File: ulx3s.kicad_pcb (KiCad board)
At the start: 4 copper layers, 139.6 x 119.6 mm, 274 parts, among them IC101 TPD4E001DRLR, IC102 74AUP1G74DC.125, IC103 CD74HC4050PWR, IC104 STM32F769IIT6, IC105 LD1117ADT33TR, IC106 N.C., IC107 IS42S16400J, IC108 AT24C256C-SSHL-B, IC109 TPS2051BDBVR, IC110 TPS61169DCKR, IC111 TPD4E001DRLR, IC112 TSC2007IPW, IC113 N.C., IC114 DP83848CVV_NOPB, J101 503398-1892, J102 67803-8020, J4 CONN_02X03, Q101 N.C., Q102 2N7002, SW101 TL1100CF160Q, SW102 PEC16-2215F-S0024, U1 LFE5U-85F-6BG381C, U10 IS25LP128F-JBLE, U3 TLV62569DBV, U4 TLV62569DBV, U5 TLV62569DBV, X101 DS1024-2*20R0, X102 DS1013-16SSIB1, X103 691322110005, X104 N.C., X105 LMJTAB881243M-L, Y1 FNETHE025, Y101 25MHz, Y102 XTAL016178-85SMX

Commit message: Adding dimensions
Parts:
- moved D20 149.3 mm to (199.9, -6.33)
- moved D21 149.3 mm to (206.2, -6.44)
- moved D23 149.3 mm to (195.1, -4.93)
- moved D24 149.3 mm to (195.1, -6.84)
- moved D25 149.3 mm to (209.7, -3.65)
- moved D26 149.3 mm to (211.6, -3.65)
- moved R52 149.3 mm to (203.8, -7.84)
- moved R53 149.3 mm to (202.4, -7.84)
- moved R54 149.3 mm to (206.0, -9.49)
- moved R63 149.3 mm to (199.9, -7.86)
- moved US2 149.3 mm to (202.7, -11.7)
- moved D9 149.3 mm to (206.7, 0.63)
- moved GPDI1 149.3 mm to (165.8, -6.75)
- moved R40 149.3 mm to (199.9, -9.25)
- moved R64 149.3 mm to (206.0, -8.09)
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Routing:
- net +5V: track 35.7 -> 258.7 mm
- net +12V: track 0.00 -> 136.6 mm
- net PE: track 0.00 -> 40.8 mm
- net GND: vias 82 -> 270
- net +3V3: vias 16 -> 37
- net USER_SW: vias 0 -> 1
- net N$124: vias 0 -> 1
- net FRM3: vias 0 -> 1
- net EOUT_B: vias 0 -> 1
- added copper zone on B.Cu, net +3V3
- added copper zone on F.Cu, net +3V3
- added copper zone on In2.Cu, net +3V3
- added copper zone on F.Cu, net +5V
- added copper zone on In2.Cu, net +5V
- added copper zone on In1.Cu, net GND
- added copper zone on F.Cu, net Net-(D2-PadA)
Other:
- board size 139.6 x 119.6 mm -> 139.5 x 70 mm
- board text added: "1"
- board text added: "1 Vdd target 2 SWCLK 3 Gnd 4 SWDIO 5 !RESET! 6 SWO"
- board text added: "2"
- board text added: "3"
- board text added: "4"
- board text added: "EEZ DIB MCU (10/2020 r3B4)"
- board text added: "EEZ DIB MCU (10/2020 r3B4) Project source code: github.com/eez-open/modular-psu"

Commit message: Combined
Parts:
- C117, C131, C133, RN2: moved to B.Cu
- moved C13 71.2 mm to (144.3, 74.0)
- moved J4 68.2 mm to (157.3, 105.5), turned to 180 degrees
- moved C1 66.4 mm to (138.8, 80.1)
- moved C2 66.4 mm to (171.2, 99.2)
- moved C3 66.4 mm to (171.4, 92.9)
- moved C30 66.4 mm to (151.2, 93.3)
- moved C4 66.4 mm to (171.4, 94.8)
- moved C42 66.4 mm to (155.1, 78.0)
- moved C46 66.4 mm to (163.2, 103.9)
- moved C48 66.4 mm to (139.1, 82.9)
- moved C53 66.4 mm to (140.7, 87.2)
- moved D28 66.4 mm to (171.7, 86.4)
- moved L3 66.4 mm to (172.7, 77.0)
- moved R11 66.4 mm to (133.9, 100.4)
- moved R27 66.4 mm to (145.4, 98.4)
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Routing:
- net +5V: track 258.7 -> 159.5 mm
- net +12V: track 136.6 -> 37.4 mm
- net JTAG_TDI: track 12.6 -> 7.73 mm, vias 3 -> 2
- net JTAG_TMS: track 11.0 -> 6.28 mm, vias 2 -> 1
- net JTAG_TCK: track 11.8 -> 7.39 mm, vias 2 -> 1
- net /gpio/OUT5V: track 4.31 -> 0.00 mm, vias 1 -> 0
- net JTAG_TDO: track 9.95 -> 5.69 mm, vias 3 -> 2
- net /gpio/IN5V: track 18.9 -> 15.3 mm
- net Net-(D26-Pad1): track 7.59 -> 4.94 mm
- net USB_FPGA_PULL_D-: track 2.47 -> 0.57 mm
- net Net-(D25-Pad2): track 4.76 -> 3.36 mm
- net 2V5_3V3: track 28.2 -> 28.0 mm, vias 4 -> 2
- net SPI2_CSB: track 0.05 -> 0.00 mm, vias 1 -> 0
- net GND: vias 270 -> 212
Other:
- board size 139.5 x 70 mm -> 139.5 x 110.4 mm

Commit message: Board update
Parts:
- C101, C103, C104, C106, C108, C109, C125, C132, C133, C135, C136, C138, C139, C151, C153, C158: footprint EEZ DIB MCU r3B4:C0805 -> Capacitor_SMD:C_0805_2012Metric
- C105, C107, C110, C111, C112, C113, C114, C116, C117, C118, C119, C120, C121, C122, C123, C124, C126, C127, C128, C129, C130, C131, C134, C137, C140, C142, C143, C144, C145, C146, C147, C148, C149, C155, C157, C159, C160, C161, C162, C163, C164, C165, C167, C168, C169, C170: footprint EEZ DIB MCU r3B4:C0603 -> Capacitor_SMD:C_0603_1608Metric
- C141, C150, C156: footprint EEZ DIB MCU r3B4:C1206 -> Capacitor_SMD:C_1206_3216Metric
- C152, C166: footprint EEZ DIB MCU r3B4:EC1206 -> Capacitor_SMD:C_1206_3216Metric
- C154: footprint EEZ DIB MCU r3B4:C1812 -> Capacitor_SMD:C_1812_4532Metric
- D20, D21, D23, D24, D25, D26, D28, D29: footprint Diode_SMD:D_SOD-323_HandSoldering -> Diode_SMD:D_SOD-323
- IC104: footprint EEZ DIB MCU r3B4:LQFP-176_24X24MM -> Package_QFP:LQFP-176_24x24mm_P0.5mm
- IC107: footprint EEZ DIB MCU r3B4:TSOPII-54 -> Package_SO:TSOP-II-54_22.2x10.16mm_P0.8mm
- R101, R102, R103, R104, R105, R106, R107, R108, R109, R110, R111, R112, R113, R114, R115, R116, R117, R118, R119, R120, R121, R122, R123, R124, R125, R126, R127, R128, R129, R130, R131, R132, R133, R134, R135, R136, R137, R138, R139, R140, R141, R142, R143, R144, R145, R146, R147, R148, R149, R150, R151: footprint EEZ DIB MCU r3B4:R0805 -> Resistor_SMD:R_0805_2012Metric
- moved R142 64.6 mm to (90.0, 50.9), turned to 270 degrees
- moved JP110 62.4 mm to (98.6, 49.6), turned to 0 degrees
- moved R140 62.0 mm to (90.0, 54.8), turned to 270 degrees
- moved JP108 60.9 mm to (98.6, 51.6), turned to 180 degrees
- moved R137 59.7 mm to (90.0, 58.8), turned to 90 degrees
- moved JP109 59.4 mm to (98.6, 53.6), turned to 180 degrees
- moved JP111 58.0 mm to (98.6, 55.6), turned to 180 degrees
- moved D21 57.3 mm to (166.3, 48.4)
- moved D23 57.3 mm to (161.1, 51.9)
- moved D25 57.3 mm to (165.3, 51.7)
- moved D26 57.3 mm to (167.2, 51.7)
- moved D9 57.3 mm to (161.6, 56.0)
- moved R52 57.3 mm to (163.9, 47.0)
- moved R53 57.3 mm to (162.5, 47.0)
- moved R54 57.3 mm to (166.2, 45.4)
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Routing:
- net +12V: track 37.4 -> 14.0 mm
- net +5V: track 159.5 -> 139.0 mm
- net +2V5: track 92.7 -> 103.0 mm
- net +3V3: track 88.4 -> 84.5 mm
- net Net-(D26-Pad1): track 4.94 -> 1.72 mm
- net USB_FPGA_PULL_D+: track 7.45 -> 5.54 mm
- net GND: vias 212 -> 202
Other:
- board size 139.5 x 110.4 mm -> 139.5 x 91.8 mm

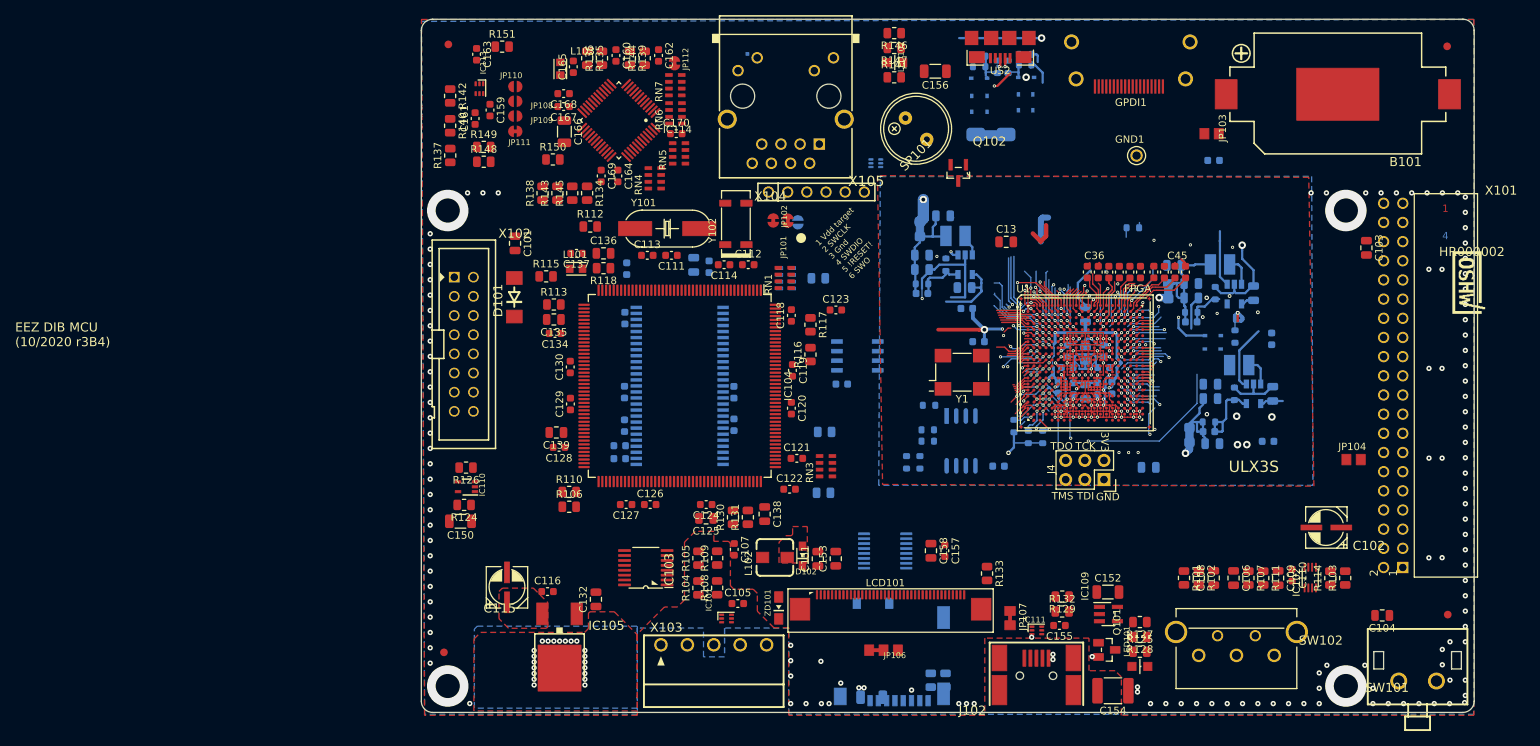
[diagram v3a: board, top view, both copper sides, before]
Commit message: Update 3D models, start to send pins to FPGA
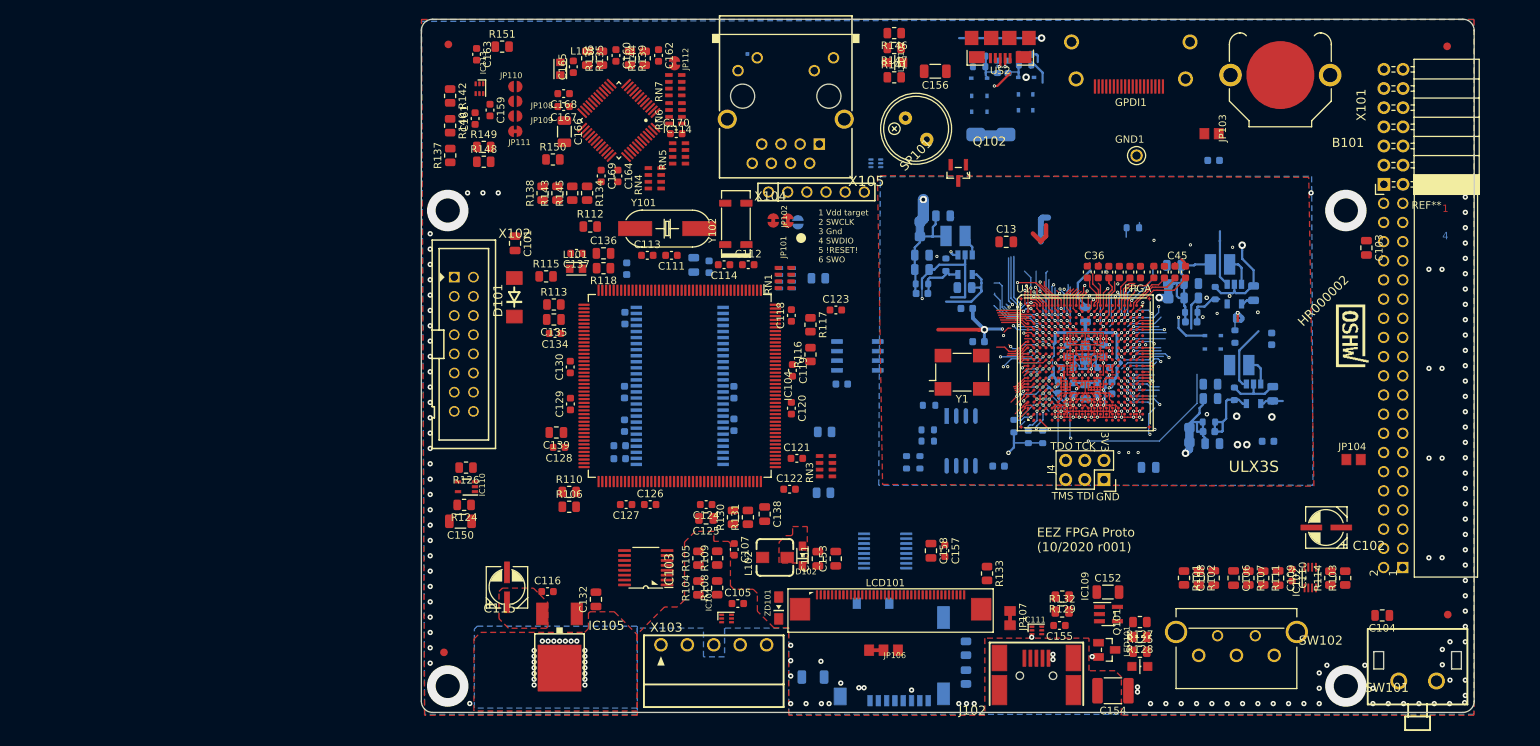
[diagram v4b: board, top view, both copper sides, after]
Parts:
- added REF**: PinSocket_2x07_P2.54mm_Horizontal, Connector_PinSocket_2.54mm:PinSocket_2x07_P2.54mm_Horizontal, F.Cu at (213.7, 62.6)
- B101: value DS1092-10-W6L -> BatteryHolder_Keystone_3001_1x12mm; footprint EEZ DIB MCU r3B4:DS1092-10-W6L -> Battery:BatteryHolder_Keystone_3001_1x12mm
- moved LABEL1 17.0 mm to (207.3, 82.7)
- moved C141 8.23 mm to (138.0, 127.9)
- moved B101 8.03 mm to (200.0, 48.1)
- moved R122 6.30 mm to (158.3, 124.1)
- moved R123 2.74 mm to (158.3, 127.9)
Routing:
- net GND: vias 202 -> 194
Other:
- board text added: "EEZ FPGA Proto (10/2020 r001)"
- board text removed: "EEZ DIB MCU (10/2020 r3B4)"

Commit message: Update
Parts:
- removed REF**: PinSocket_2x07_P2.54mm_Horizontal, Connector_PinSocket_2.54mm:PinSocket_2x07_P2.54mm_Horizontal
- removed RN1, RN2, RN7: DR1206-33R-4/8, EEZ DIB MCU r3B4:CAY16
- added H1: HOLE, MountingHole:MountingHole_3.2mm_M3_ISO14580_Pad, F.Cu at (89.7, 66.2)
- added H2: HOLE, MountingHole:MountingHole_3.2mm_M3_ISO14580_Pad, F.Cu at (208.6, 66.2)
- added H3: HOLE, MountingHole:MountingHole_3.2mm_M3_ISO14580_Pad, F.Cu at (208.6, 129.1)
- added H4: HOLE, MountingHole:MountingHole_3.2mm_M3_ISO14580_Pad, F.Cu at (89.5, 129.1)
- added RN101: DR1206-33R-4/8, EEZ DIB MCU r3B4:CAY16, F.Cu at (134.3, 75.0)
- added RN102: DR1206-33R-4/8, EEZ DIB MCU r3B4:CAY16, B.Cu at (134.4, 75.0)
- added RN103: DR1206-33R-4/8, EEZ DIB MCU r3B4:CAY16, F.Cu at (109.1, 108.5)
- added RN107: DR1206-33R-4/8, EEZ DIB MCU r3B4:CAY16, F.Cu at (102.7, 68.4)
- B101: value BatteryHolder_Keystone_3001_1x12mm -> DS1092-10-W6L; footprint Battery:BatteryHolder_Keystone_3001_1x12mm -> EEZ DIB MCU r3B4:DS1092-10-W6L
- C152: footprint Capacitor_SMD:C_1206_3216Metric -> Capacitor_Tantalum_SMD:CP_EIA-3216-10_Kemet-I
- C166: value 10u -> 10uF; footprint Capacitor_SMD:C_1206_3216Metric -> Capacitor_Tantalum_SMD:CP_EIA-3216-10_Kemet-I
- R101, R102, R103, R104, R105, R106, R107, R108, R109, R110, R111, R112, R113, R114, R115, R122, R123, R124, R125, R126, R127, R128, R132, R133, R137, R146, R147: footprint Resistor_SMD:R_0805_2012Metric -> Resistor_SMD:R_0603_1608Metric
- RN105: renamed from RN5; moved to B.Cu
- moved R149 28.6 mm to (123.0, 59.5), turned to 45 degrees
- moved IC113 24.3 mm to (112.8, 65.1), turned to 180 degrees
- moved R116 22.8 mm to (151.2, 66.8), turned to 180 degrees
- moved RN106 20.4 mm to (106.2, 68.4), turned to 180 degrees
- moved IC112 19.9 mm to (166.8, 116.3), turned to 0 degrees
- moved R117 18.3 mm to (151.4, 69.1), turned to 180 degrees
- moved R112 16.8 mm to (119.5, 55.5)
- moved R134 15.2 mm to (120.0, 54.2), turned to 0 degrees
- moved C157 14.5 mm to (142.5, 104.8)
- moved C123 12.6 mm to (146.6, 68.0)
- moved R133 11.8 mm to (172.9, 113.9)
- moved C158 11.5 mm to (142.5, 108.3)
- moved RN104 9.67 mm to (110.1, 68.4), turned to 0 degrees
- moved C11 8.49 mm to (150.6, 82.2)
- moved C17 8.49 mm to (172.2, 98.3)
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- renumbered RN4 to RN104, RN6 to RN106
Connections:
- C152 pad 1: (no net) -> Net-(C152-Pad1)
- C152 pad 2: (no net) -> GND
- C155 pad 2: Net-(C152-Pad+) -> Net-(C152-Pad1)
- C166 pad 1: (no net) -> Net-(C164-Pad1)
- C166 pad 2: (no net) -> GND
- IC104 pad 11: LTDC_VSYNC -> LED3
- IC104 pad 114: LTDC_R7 -> LED1
- IC104 pad 115: LTDC_CLK -> GP12
- IC104 pad 12: LTDC_HSYNC -> LED2
- IC104 pad 121: SDMMC1_D0 -> (no net)
- IC104 pad 123: SPI2_IRQ -> (no net)
- IC104 pad 13: LTDC_G6 -> LED0
- IC104 pad 132: LTDC_G5 -> GP11
- IC104 pad 138: SPI5_IRQ -> (no net)
- IC104 pad 141: SDMMC1_CK -> (no net)
- IC104 pad 144: SDMMC1_CMD -> (no net)
- IC104 pad 145: LTDC_G7 -> GP9
- IC104 pad 153: LTDC_G3 -> GP10
- IC104 pad 154: LTDC_B3 -> GN11
- IC104 pad 155: LTDC_B4 -> AUDIO_V2
- IC104 pad 156: SPI5_CSB -> (no net)
- IC104 pad 157: SD_DETECT -> (no net)
- IC104 pad 160: FMC_SDNCAS -> (no net)
- IC104 pad 168: SPI4_IRQ -> (no net)
- IC104 pad 174: LTDC_B5 -> AUDIO_R2
- IC104 pad 175: LTDC_B6 -> AUDIO_L1
- IC104 pad 176: LTDC_B7 -> GN10
- IC104 pad 28: LTDC_DE -> AUDIO_L0
- IC104 pad 32: LTDC_R5 -> LED6
- IC104 pad 4: SPI4_MISO -> (no net)
- IC104 pad 45: LTDC_G4 -> AUDIO_L2
- IC104 pad 51: LTDC_R4 -> LED4
- IC104 pad 52: LTDC_G2 -> AUDIO_R0
- IC104 pad 56: LTDC_R3 -> LED7
- IC104 pad 57: LTDC_R6 -> GN9
- IC104 pad 87: SPI2_MISO -> (no net)
- IC107 pad 17: FMC_SDNCAS -> (no net)
- IC109 pad 1: Net-(C152-Pad+) -> Net-(C152-Pad1)
- IC111 pad 6: Net-(C152-Pad+) -> Net-(C152-Pad1)
- J101 pad 3: SDMMC1_CMD -> SDMMC1_FROM_FPGA_CMD
- J101 pad 5: SDMMC1_CK -> (no net)
- J101 pad 7: SDMMC1_D0 -> SDMMC1_FROM_FPGA_D0
- J101 pad SW1: SD_DETECT -> (no net)
- J102 pad 1: Net-(C152-Pad+) -> Net-(C152-Pad1)
- LCD101 pad 10: LTDC_R5 -> FTDI_nRXLED
- LCD101 pad 11: LTDC_R6 -> LTDC_FROM_FPGA_R6
- LCD101 pad 12: LTDC_R7 -> LTDC_FROM_FPGA_R7
- LCD101 pad 15: LTDC_G2 -> FTDI_TXDEN
- LCD101 pad 16: LTDC_G3 -> LTDC_FROM_FPGA_G3
- LCD101 pad 17: LTDC_G4 -> LTDC_FROM_FPGA_G4
- LCD101 pad 18: LTDC_G5 -> FTDI_RXD
- LCD101 pad 19: LTDC_G6 -> LTDC_FROM_FPGA_G6
- LCD101 pad 20: LTDC_G7 -> LTDC_FROM_FPGA_G7
- LCD101 pad 24: LTDC_B3 -> LTDC_FROM_FPGA_B3
- LCD101 pad 25: LTDC_B4 -> LTDC_FROM_FPGA_B4
- LCD101 pad 26: LTDC_B5 -> LTDC_FROM_FPGA_B5
- LCD101 pad 27: LTDC_B6 -> LTDC_FROM_FPGA_B6
- LCD101 pad 28: LTDC_B7 -> LTDC_FROM_FPGA_B7
- LCD101 pad 30: LTDC_CLK -> LTDC_FROM_FPGA_CLK
- LCD101 pad 32: LTDC_HSYNC -> BTN_L
- LCD101 pad 33: LTDC_VSYNC -> BTN_D
- LCD101 pad 34: LTDC_DE -> LTDC_FROM_FPGA_DE
- LCD101 pad 8: LTDC_R3 -> LTDC_FROM_FPGA_R3
- LCD101 pad 9: LTDC_R4 -> LTDC_FROM_FPGA_R4
- R122 pad 2: SDMMC1_D0 -> SDMMC1_FROM_FPGA_D0
- R123 pad 2: SDMMC1_CMD -> SDMMC1_FROM_FPGA_CMD
- R128 pad 1: Net-(C152-Pad+) -> Net-(C152-Pad1)
- R129 pad 1: Net-(C152-Pad+) -> Net-(C152-Pad1)
- RN3 pad 1: SPI2_CSB -> (no net)
- RN3 pad 2: SPI2_CLK -> (no net)
- RN3 pad 3: SPI2_MOSI -> (no net)
- RN3 pad 4: SPI2_CSA -> (no net)
- RN3 pad 5: Net-(IC104-Pad162) -> (no net)
- U1 pad A2: (no net) -> GP9
- U1 pad A3: (no net) -> AUDIO_R0
- U1 pad B1: (no net) -> GN9
- U1 pad B2: (no net) -> LED0
- U1 pad B4: (no net) -> GN10
- U1 pad C1: (no net) -> LED2
- U1 pad C2: (no net) -> LED1
- U1 pad C3: (no net) -> AUDIO_L2
- U1 pad C4: (no net) -> GP10
- U1 pad D1: (no net) -> LED4
- U1 pad D2: (no net) -> LED3
- U1 pad D3: (no net) -> AUDIO_L1
- U1 pad D5: (no net) -> AUDIO_R2
- U1 pad E1: (no net) -> LED6
- U1 pad E3: (no net) -> GN11
- U1 pad E4: (no net) -> AUDIO_L0
- U1 pad F4: (no net) -> GP11
- U1 pad F5: (no net) -> AUDIO_V2
- U1 pad G1: (no net) -> LTDC_FROM_FPGA_R3
- U1 pad G3: (no net) -> GP12
- U1 pad H1: (no net) -> LTDC_FROM_FPGA_G3
- U1 pad H3: (no net) -> LED7
- U1 pad J1: (no net) -> LTDC_FROM_FPGA_R6
- U1 pad J4: (no net) -> LTDC_FROM_FPGA_CLK
- U1 pad J5: (no net) -> LTDC_FROM_FPGA_R4
- U1 pad K1: (no net) -> LTDC_FROM_FPGA_R7
- U1 pad K2: (no net) -> LTDC_FROM_FPGA_G4
- U1 pad K4: (no net) -> LTDC_FROM_FPGA_G6
- U1 pad L1: (no net) -> LTDC_FROM_FPGA_B4
- U1 pad L3: (no net) -> FTDI_TXDEN
- U1 pad L4: (no net) -> FTDI_RXD
- U1 pad L5: (no net) -> FTDI_nRXLED
- U1 pad N2: (no net) -> LTDC_FROM_FPGA_B6
- U1 pad N3: (no net) -> LTDC_FROM_FPGA_B3
- U1 pad N4: (no net) -> LTDC_FROM_FPGA_G7
- U1 pad N5: (no net) -> LTDC_FROM_FPGA_DE
- U1 pad P1: (no net) -> LTDC_FROM_FPGA_B7
- U1 pad P3: (no net) -> LTDC_FROM_FPGA_B5
- U1 pad U1: (no net) -> BTN_L
- U1 pad V1: (no net) -> BTN_D
- X101 pad 11: SPI5_CSA -> (no net)
- X101 pad 13: SPI5_CSB -> (no net)
- X101 pad 17: SPI5_CLK -> (no net)
- X101 pad 18: SPI5_MISO -> (no net)
- X101 pad 19: SPI4_IRQ -> (no net)
- X101 pad 20: SPI5_MOSI -> (no net)
- X101 pad 21: SPI4_CSB -> (no net)
- X101 pad 22: SPI4_CSA -> (no net)
- X101 pad 23: SPI4_CLK -> (no net)
- X101 pad 24: SPI4_MISO -> (no net)
- X101 pad 25: SPI2_IRQ -> (no net)
- X101 pad 26: SPI4_MOSI -> (no net)
- X101 pad 27: SPI2_CSB -> (no net)
- X101 pad 28: SPI2_CSA -> (no net)
- X101 pad 31: SPI2_MISO -> (no net)
- X101 pad 32: SPI2_CLK -> (no net)
- X101 pad 33: SPI2_MOSI -> (no net)
- X101 pad 9: SPI5_IRQ -> (no net)
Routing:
- net (no net): track 669.1 -> 405.3 mm, vias 138 -> 91
- net AUDIO_V2: track 0.00 -> 13.5 mm, vias 0 -> 2
- net /flash/FLASH_nHOLD: track 0.94 -> 13.3 mm, vias 0 -> 1
- net /flash/FLASH_nCS: track 3.25 -> 15.6 mm, vias 0 -> 1
- net LTDC_TO_FPGA_B3: track 0.00 -> 12.0 mm, vias 0 -> 1
- net /flash/FLASH_SCK: track 3.62 -> 14.7 mm
- net /flash/FLASH_MISO: track 2.49 -> 13.3 mm
- net LTDC_TO_FPGA_G6: track 0.00 -> 10.7 mm, vias 0 -> 1
- net USER_PROGRAMN: track 0.00 -> 10.2 mm, vias 0 -> 1
- net AUDIO_L2: track 0.00 -> 9.65 mm, vias 0 -> 1
- net /flash/FLASH_MOSI: track 2.98 -> 12.4 mm
- net /flash/FLASH_nWP: track 2.98 -> 12.0 mm, vias 1 -> 2
- net GP10: track 0.00 -> 8.87 mm, vias 0 -> 2
- net AUDIO_L1: track 0.00 -> 8.52 mm, vias 0 -> 1
- net AUDIO_L0: track 0.00 -> 8.20 mm, vias 0 -> 1
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
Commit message: PCB update
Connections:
- net GP10 renamed LTDC_TO_FPGA_G3
- IC104 pad 13: LED0 -> LTDC_TO_FPGA_G6
- IC104 pad 160: (no net) -> FMC_SDNCAS
- IC107 pad 17: (no net) -> FMC_SDNCAS
- U1 pad B2: LED0 -> LTDC_TO_FPGA_G6
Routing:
- net (no net): track 405.3 -> 433.2 mm, vias 91 -> 92
- net LTDC_TO_FPGA_B3: track 12.0 -> 0.00 mm, vias 1 -> 0
- net LTDC_FROM_FPGA_HSYNC: track 6.39 -> 0.00 mm, vias 1 -> 0
- net AUDIO_L2: track 9.65 -> 4.21 mm
- net LTDC_TO_FPGA_G6: track 10.7 -> 5.30 mm, vias 1 -> 2
- net LED0: track 5.30 -> 0.00 mm, vias 2 -> 0
- net AUDIO_L1: track 8.52 -> 4.68 mm
- net GN11: track 5.51 -> 2.99 mm
- net AUDIO_L0: track 8.20 -> 5.82 mm
